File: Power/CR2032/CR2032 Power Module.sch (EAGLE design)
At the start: 3 parts

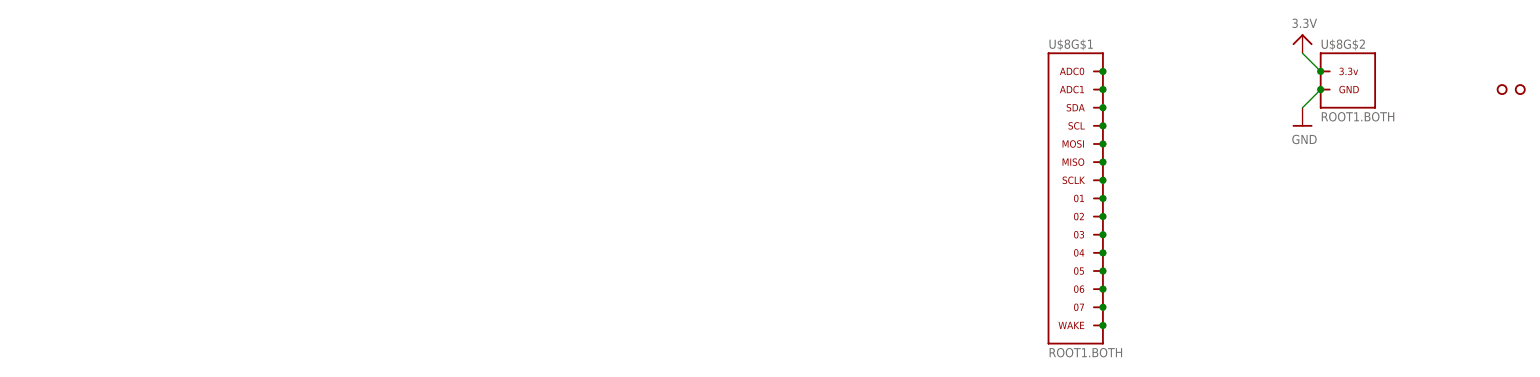
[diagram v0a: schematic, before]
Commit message: Created CR2032 Power Module project.
Signed-off-by: Cruz Monrreal II <Cruz.Monrreal@gmail.com>
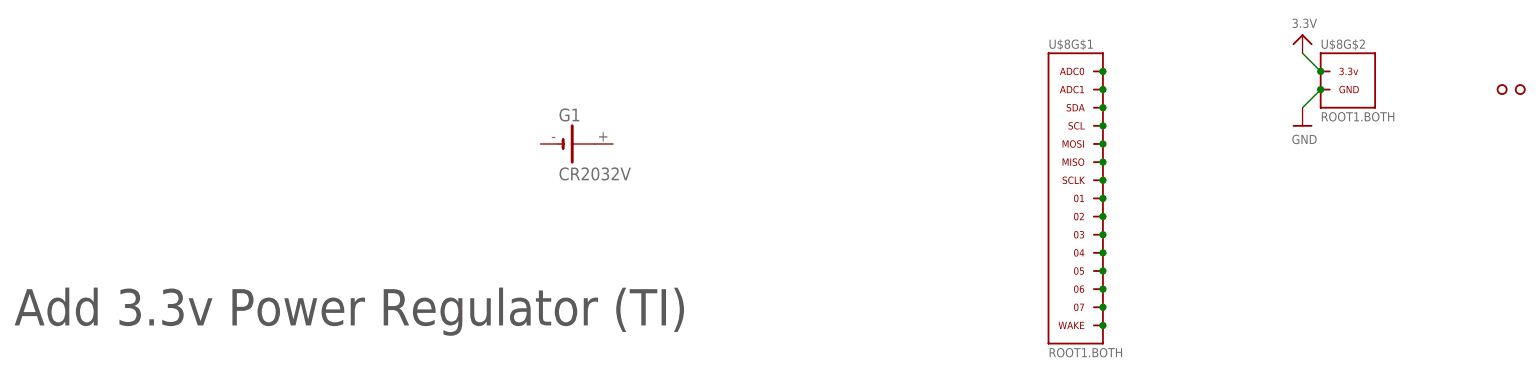
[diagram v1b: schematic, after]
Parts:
- added G1: CR2032V, battery:CR2032V
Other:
- note added: "Add 3.3v Power Regulator (TI)"
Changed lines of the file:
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@@
 <part name="U$3" library=".screw_holes" deviceset="HOLE" device=".2MM"/>
 <part name="U$8" library="thinkmaketest" deviceset="ROOT1" device=".BOTH"/>
+<part name="G1" library="battery" deviceset="CR2032V" device=""/>
 </parts>
 <sheets>
 <sheet>
 <plain>
+<text x="22.86" y="93.98" size="5.08" layer="97">Add 3.3v Power Regulator (TI)</text>
 </plain>
 <instances>
@@
 <instance part="U$8" gate="G$1" x="172.72" y="111.76"/>
 <instance part="U$8" gate="G$2" x="210.82" y="127"/>
+<instance part="G1" gate="1" x="101.6" y="119.38"/>
 </instances>
 <busses>
